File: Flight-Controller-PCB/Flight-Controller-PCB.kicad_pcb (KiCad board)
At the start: 2 copper layers, 50 x 50 mm, 69 parts, among them J1 Power_In, J2 ESC_1, J3 ESC_2, J4 ESC_3, J5 ESC_4, J6 Receiver, J7 Aux, J8 USB_B_Micro, J9 ICSP, Q1 BSS138, Q2 BSS138, SW1 Reset, U1 MCP6001U, U2 ICM-20689, U3 FT232RL, U4 ATmega328P-AU, U5 LM1117-5.0, Y1 16 MHz

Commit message: Power Management and Selection roughed out
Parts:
- removed the C10 at (95.2, 110.5)
- removed the C18 at (95.2, 116.8)
- removed the D2 at (92.4, 99.3)
- removed the D3 at (94.1, 99.3)
- removed D5: Green 2.2V 20mA, LED_SMD:LED_0603_1608Metric_Pad1.05x0.95mm_HandSolder
- removed J9: ICSP, Connector_PinHeader_2.54mm:PinHeader_2x03_P2.54mm_Vertical
- removed the R16 at (92.4, 103.0)
- removed the R17 at (94.2, 103.0)
- removed R21: 1 kohm 5%, Resistor_SMD:R_0603_1608Metric_Pad1.05x0.95mm_HandSolder
- removed R22: 200 ohm 5%, Resistor_SMD:R_0603_1608Metric_Pad1.05x0.95mm_HandSolder
- removed SW1: Reset, Custom:Switch
- added C13: 1uF 16V X7R 10%, Capacitor_SMD:C_0603_1608Metric_Pad1.05x0.95mm_HandSolder, F.Cu at (156.7, 124.2)
- added C7: 22pF 12V X7R 2%, Capacitor_SMD:C_0603_1608Metric_Pad1.05x0.95mm_HandSolder, F.Cu at (154.2, 119.1)
- added R19: 22 ohm 1%, Resistor_SMD:R_0603_1608Metric_Pad1.05x0.95mm_HandSolder, F.Cu at (133.7, 123.4)
- added R20: 22 ohm 1%, Resistor_SMD:R_0603_1608Metric_Pad1.05x0.95mm_HandSolder, F.Cu at (131.8, 120.1)
- added Y1: 16MHz, CL 7pF, Custom:Crystal, F.Cu at (150.9, 125.0)
- C11: value 0.1uF 16V X7R 10% -> 22pF 12V X7R 2%
- U3: value FT232RL -> ATmega32U4-AU; footprint Package_SO:SSOP-28_5.3x10.2mm_P0.65mm -> Package_QFP:TQFP-44_10x10mm_P0.8mm
- moved U3 41.5 mm to (142.5, 116.3), turned to 45 degrees
- moved C11 38.4 mm to (145.3, 126.5), turned to 0 degrees
- renumbered C9 to C10, C13 to C14, C14 to C15, C15 to C16, C16 to C17, C17 to C18, C7 to C8, C8 to C9, D4 to D2, D6 to D3, R18 to R16, R19 to R17, R20 to R18, U5 to U4, Y1 to Y2
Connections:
- net Net-(D1-Pad1) renamed /B_RGB
- net Net-(D1-Pad3) renamed /R_RGB
- net Net-(D1-Pad5) renamed /G_RGB
- C11 pad 1: RESET -> GND
- J6 pad 4: D11 -> Aux_Digital
- J6 pad 6: (no net) -> Aux_Digital
- J7 pad 2: A6 -> A1
- R16 pad 1: RX -> (no net)
- R16 pad 2: Net-(R18-Pad2) -> (no net)
- R17 pad 1: TX -> (no net)
- R17 pad 2: Net-(R19-Pad2) -> (no net)
- R4 pad 1: D12 -> D2
- R5 pad 1: D2 -> (no net)
- R6 pad 1: A1 -> A2
- R7 pad 1: A2 -> A3
- R8 pad 1: A3 -> A6
- U3 pad 1: RX -> (no net)
- U3 pad 14: (no net) -> Net-(U3-Pad14)
- U3 pad 15: Net-(J8-Pad3) -> GND
- U3 pad 16: Net-(J8-Pad2) -> Net-(C11-Pad2)
- U3 pad 17: +3V3 -> Net-(C7-Pad1)
- U3 pad 18: GND -> (no net)
- U3 pad 2: Net-(C11-Pad2) -> (no net)
- U3 pad 20: +5V -> (no net)
- U3 pad 21: GND -> (no net)
- U3 pad 22: Net-(D3-Pad1) -> (no net)
- U3 pad 23: Net-(D2-Pad1) -> GND
- U3 pad 24: (no net) -> Net-(U3-Pad24)
- U3 pad 25: GND -> (no net)
- U3 pad 26: GND -> (no net)
- U3 pad 3: (no net) -> D-
- U3 pad 4: +5V -> D+
- U3 pad 5: TX -> GND
- U3 pad 6: (no net) -> Net-(C13-Pad1)
- U3 pad 7: GND -> (no net)
- U4 pad 15: D11 -> (no net)
- U4 pad 16: D12 -> (no net)
- U4 pad 29: RESET -> (no net)
- U4 pad 30: Net-(R18-Pad2) -> (no net)
- U4 pad 31: Net-(R19-Pad2) -> (no net)
- U4 pad 7: Net-(U4-Pad7) -> (no net)
- U4 pad 8: Net-(U4-Pad8) -> (no net)
- Y2 pad 1: Net-(U4-Pad8) -> (no net)
- Y2 pad 3: Net-(U4-Pad7) -> (no net)
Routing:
- net (no net): track 0.00 -> 122.8 mm, vias 0 -> 7
- net D12: track 57.1 -> 0.00 mm, vias 3 -> 0
- net RESET: track 40.9 -> 0.00 mm, vias 2 -> 0
- net D2: track 21.7 -> 50.9 mm, vias 2 -> 4
- net D11: track 28.7 -> 0.00 mm, vias 2 -> 0
- net Aux_Digital: track 65.1 -> 91.4 mm, vias 3 -> 5
- net Net-(R19-Pad2): track 22.0 -> 0.00 mm, vias 2 -> 0
- net Net-(R18-Pad2): track 14.0 -> 0.00 mm, vias 2 -> 0
- net A6: track 7.56 -> 0.00 mm
- net A1: track 0.00 -> 7.56 mm
- net RX: track 6.81 -> 0.00 mm
- net TX: track 6.71 -> 0.00 mm
- net Net-(U4-Pad8): track 2.82 -> 0.00 mm
- net Net-(U4-Pad7): track 2.81 -> 0.00 mm
- net Net-(D2-Pad2) (its old number): track 1.96 -> 0.00 mm
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
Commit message: Create BOM and schematic
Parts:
- removed the U4 at (88.9, 126.4)
- removed the U4 at (101.9, 103.4)
- removed Y2: 16 MHz, Custom:Resonator
- added C19: 22uF 16V 20%, Capacitor_SMD:C_0603_1608Metric_Pad1.05x0.95mm_HandSolder, F.Cu at (185.8, 138.7)
- added C20: 22uF 16V 20%, Capacitor_SMD:C_0603_1608Metric_Pad1.05x0.95mm_HandSolder, F.Cu at (190.1, 139.0)
- added C21: 0.1uF 16V X7R 10%, Capacitor_SMD:C_0603_1608Metric_Pad1.05x0.95mm_HandSolder, F.Cu at (199.7, 129.5)
- added C22: 1uF 16V X7R 10%, Capacitor_SMD:C_0603_1608Metric_Pad1.05x0.95mm_HandSolder, F.Cu at (196.3, 124.5)
- added D4: 75V 150mA, Diode_SMD:D_0603_1608Metric_Pad1.05x0.95mm_HandSolder, F.Cu at (186.6, 133.7)
- added D5: Orange 2V 20mA, LED_SMD:LED_0603_1608Metric_Pad1.05x0.95mm_HandSolder, F.Cu at (186.7, 126.4)
- added D6: Orange 2V 20mA, LED_SMD:LED_0603_1608Metric_Pad1.05x0.95mm_HandSolder, F.Cu at (177.1, 139.7)
- added FB1: Ferrite 30 ohm 1 line, Diode_SMD:D_0603_1608Metric_Pad1.05x0.95mm_HandSolder, F.Cu at (178.2, 135.8)
- added J9: USB_B_Micro, Connector_USB:USB_Micro-B_Molex-105017-0001, F.Cu at (179.5, 123.6)
- added Q3: PMV48XP,215, Package_TO_SOT_SMD:SOT-23, F.Cu at (186.6, 130.1)
- added Q4: PMV48XP,215, Package_TO_SOT_SMD:SOT-23, F.Cu at (191.9, 122.9)
- added R21: 22 ohm 1%, Resistor_SMD:R_0603_1608Metric_Pad1.05x0.95mm_HandSolder, F.Cu at (190.1, 136.5)
- added RV1: 5V 0.5pF, Diode_SMD:D_0603_1608Metric_Pad1.05x0.95mm_HandSolder, F.Cu at (177.1, 142.3)
- added RV2: 5V 0.5pF, Diode_SMD:D_0603_1608Metric_Pad1.05x0.95mm_HandSolder, F.Cu at (196.3, 122.0)
- added SW1: Push-Switch, Custom:Switch, F.Cu at (179.5, 131.2)
- added U4: LM1117-5.0, Package_TO_SOT_SMD:SOT-223, F.Cu at (165.1, 139.2)
- added U5: LP2985-3.3, Package_TO_SOT_SMD:SOT-23-5, F.Cu at (172.4, 140.7)
- C11: value 22pF 12V X7R 2% -> 1uF 16V X7R 10%
- C12, C18: value 0.1uF 16V X7R 10% -> 1uF 16V X7R 10%
- C13: value 1uF 16V X7R 10% -> 0.1uF 16V X7R 10%
- C14, C15: value 10uF 25V 20% -> 0.1uF 16V X7R 10%
- C16: value 1uF 16V X7R 10% -> 0.1uF 20V X7R 10%
- C17: value 4.7uF 10V 20% -> 10uF 20V 20%
- C4: value 2.2uF 16V X7R 10% -> 0.47uF 16V X7R 10%
- C5: value 0.1uF 16V X7R 10% -> 2.2uF 16V X7R 10%
- C6: value 0.47uF 16V X7R 10% -> 0.1uF 16V X7R 10%
- C8: value 1uF 16V X7R 10% -> 22pF 12V X7R 2%
- C9: value 4.7uF 10V 20% -> 0.1uF 16V X7R 10%
- D3: value SS1P3L -> Green 2.2V 20mA; footprint Custom:SS1P3L -> LED_SMD:LED_0603_1608Metric_Pad1.05x0.95mm_HandSolder
- J1: value Power_In -> ESC_1; footprint Connector_JST:JST_GH_BM06B-GHS-TBT_1x06-1MP_P1.25mm_Vertical -> Connector_JST:JST_GH_BM05B-GHS-TBT_1x05-1MP_P1.25mm_Vertical
- J2: value ESC_1 -> Receiver; footprint Connector_JST:JST_GH_BM04B-GHS-TBT_1x04-1MP_P1.25mm_Vertical -> Connector_JST:JST_GH_BM07B-GHS-TBT_1x07-1MP_P1.25mm_Vertical
- J3: footprint Connector_JST:JST_GH_BM04B-GHS-TBT_1x04-1MP_P1.25mm_Vertical -> Connector_JST:JST_GH_BM05B-GHS-TBT_1x05-1MP_P1.25mm_Vertical
- J4: value ESC_3 -> ICSP; footprint Connector_JST:JST_GH_BM04B-GHS-TBT_1x04-1MP_P1.25mm_Vertical -> Connector_PinHeader_2.54mm:PinHeader_2x03_P2.54mm_Vertical
- J5: value ESC_4 -> ESC_3; footprint Connector_JST:JST_GH_BM04B-GHS-TBT_1x04-1MP_P1.25mm_Vertical -> Connector_JST:JST_GH_BM05B-GHS-TBT_1x05-1MP_P1.25mm_Vertical
- J6: value Receiver -> Aux; footprint Connector_JST:JST_GH_BM07B-GHS-TBT_1x07-1MP_P1.25mm_Vertical -> Connector_JST:JST_GH_BM04B-GHS-TBT_1x04-1MP_P1.25mm_Vertical
- J7: value Aux -> ESC_4; footprint Connector_JST:JST_GH_BM04B-GHS-TBT_1x04-1MP_P1.25mm_Vertical -> Connector_JST:JST_GH_BM05B-GHS-TBT_1x05-1MP_P1.25mm_Vertical
- J8: value USB_B_Micro -> Power_In; footprint Connector_USB:USB_Micro-B_Molex-105017-0001 -> Connector_JST:JST_GH_BM06B-GHS-TBT_1x06-1MP_P1.25mm_Vertical
- R15: value 10 kohm 5% -> 1 kohm 5%
- R17: value 1 kohm 5% -> 10 kohm 5%
- R18: value 150 ohm 5% -> 10 kohm 5%
- R19: value 22 ohm 1% -> 10 kohm 5%
- R6: value ?? ohm 5% -> 150 ohm 5%
- R7: value ?? ohm 5% -> 55 ohm 5%
- R8, R9: value ?? ohm 5% -> 10 kohm 5%
- moved R15 116.8 mm to (200.6, 124.5), turned to 0 degrees
- moved R14 112.4 mm to (195.4, 127.0)
- moved C9 109.3 mm to (191.0, 126.5), turned to 0 degrees
- moved C8 109.2 mm to (191.0, 129.0)
- moved C14 106.2 mm to (194.5, 137.1)
- moved C10 106.0 mm to (200.7, 121.9), turned to 0 degrees
- moved R18 105.8 mm to (181.4, 143.4), turned to 0 degrees
- moved C12 104.9 mm to (199.7, 132.0), turned to 0 degrees
- moved C15 102.9 mm to (195.3, 132.0), turned to 0 degrees
- moved U1 102.7 mm to (177.3, 94.5), turned to 0 degrees
- moved C1 98.1 mm to (177.1, 98.1), turned to 0 degrees
- moved R16 97.7 mm to (195.3, 129.5), turned to 0 degrees
- moved C16 97.0 mm to (191.0, 131.5), turned to 0 degrees
- moved R1 94.6 mm to (170.3, 110.8), turned to 0 degrees
- moved C2 93.6 mm to (171.3, 103.7), turned to 0 degrees
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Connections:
- C10 pad 1: +5V -> Net-(C10-Pad1)
- C11 pad 1: GND -> +5V
- C11 pad 2: Net-(C11-Pad2) -> GND
- C12 pad 1: Net-(C12-Pad1) -> +5V
- C13 pad 1: Net-(C13-Pad1) -> +5V
- C14 pad 1: VDD -> +5V
- C15 pad 1: +5V -> VBUS
- C16 pad 1: +5V -> Net-(C16-Pad1)
- C17 pad 1: VBUS -> Net-(C16-Pad1)
- C18 pad 1: VBUS -> +5V
- C4 pad 1: +3V3 -> Net-(C4-Pad1)
- C5 pad 1: GND -> +3V3
- C5 pad 2: +3V3 -> GND
- C6 pad 1: Net-(C6-Pad1) -> GND
- C6 pad 2: GND -> +3V3
- C8 pad 2: +5V -> Net-(C8-Pad2)
- C9 pad 1: +5V -> Net-(C9-Pad1)
- D3 pad 1: +5V -> GND
- D3 pad 2: VBUS -> Net-(D3-Pad2)
- F1 pad 1: Net-(F1-Pad1) -> Net-(C20-Pad1)
- J1 pad 2: GND -> A1
- J1 pad 4: VDD -> D4
- J1 pad 5: VDD -> +5V
- J2 pad 2: Net-(J2-Pad2) -> D15-SCK
- J2 pad 3: D4 -> D16-MOSI
- J2 pad 4: +5V -> D8
- J3 pad 2: Net-(J3-Pad2) -> A2
- J3 pad 3: D5 -> GND
- J3 pad 4: +5V -> D5
- J4 pad 1: GND -> D14-MISO
- J4 pad 2: Net-(J4-Pad2) -> +5V
- J4 pad 3: D6 -> D15-SCK
- J4 pad 4: +5V -> D16-MOSI
- J5 pad 2: Net-(J5-Pad2) -> A3
- J5 pad 3: D7 -> GND
- J5 pad 4: +5V -> D6
- J6 pad 2: D8 -> A5
- J6 pad 3: D9 -> Aux_Digital
- J6 pad 4: Aux_Digital -> +5V
- J7 pad 2: A1 -> A4
- J7 pad 3: Aux_Digital -> GND
- J7 pad 4: +5V -> D7
- J8 pad 1: Net-(F1-Pad1) -> GND
- J8 pad 2: Net-(J8-Pad2) -> GND
- J8 pad 3: Net-(J8-Pad3) -> GND
- J8 pad 4: (no net) -> VDD
- J8 pad 5: GND -> VDD
- J8 pad 6: GND -> VDD
- Q1 pad 3: A5_SCL -> IMU_SCL_LH
- Q2 pad 3: A4_SDA -> IMU_SDA_LH
- R10 pad 1: IMU_SCL_LL -> IMU_SCL_LH
- R10 pad 2: +3V3 -> +5V
- R11 pad 1: IMU_SCL_LL -> IMU_SDA_LL
- R12 pad 1: A5_SCL -> IMU_SDA_LL
- R12 pad 2: +5V -> +3V3
- R13 pad 1: IMU_SDA_LL -> IMU_SDA_LH
- R13 pad 2: +3V3 -> +5V
- R14 pad 1: IMU_SDA_LL -> RESET
- R14 pad 2: +3V3 -> +5V
- R15 pad 1: A4_SDA -> Net-(R15-Pad1)
- R15 pad 2: +5V -> Net-(D5-Pad2)
- R16 pad 1: (no net) -> Net-(R16-Pad1)
- R16 pad 2: (no net) -> Net-(D6-Pad2)
- R17 pad 1: (no net) -> Net-(R17-Pad1)
- R17 pad 2: (no net) -> GND
- R18 pad 1: Net-(D2-Pad2) -> GND
- R18 pad 2: +5V -> VDD
- R19 pad 1: Net-(J8-Pad3) -> GND
- R19 pad 2: D+ -> VBUS
- R20 pad 1: D- -> D+
- R20 pad 2: Net-(J8-Pad2) -> D+
- R4 pad 1: D2 -> D11
- R5 pad 1: (no net) -> D12
- R6 pad 1: A2 -> +5V
- R6 pad 2: Net-(J2-Pad2) -> Net-(D2-Pad2)
- R7 pad 1: A3 -> +3V3
- R7 pad 2: Net-(J3-Pad2) -> Net-(D3-Pad2)
- R8 pad 1: A6 -> IMU_SCL_LL
- R8 pad 2: Net-(J4-Pad2) -> +3V3
- R9 pad 1: A7 -> IMU_SCL_LL
- R9 pad 2: Net-(J5-Pad2) -> +3V3
- U2 pad 10: Net-(C6-Pad1) -> Net-(C4-Pad1)
- U2 pad 12: (no net) -> Net-(U2-Pad12)
- U2 pad 22: (no net) -> Net-(U2-Pad22)
- U3 pad 1: (no net) -> D7
- U3 pad 10: (no net) -> D16-MOSI
- U3 pad 11: (no net) -> D14-MISO
- U3 pad 12: (no net) -> D11
- U3 pad 13: (no net) -> RESET
- U3 pad 14: Net-(U3-Pad14) -> +5V
- U3 pad 16: Net-(C11-Pad2) -> Net-(C8-Pad2)
- U3 pad 18: (no net) -> IMU_SCL_LH
- U3 pad 19: (no net) -> IMU_SDA_LH
- U3 pad 2: (no net) -> +5V
- U3 pad 20: (no net) -> RX
- U3 pad 21: (no net) -> TX
- U3 pad 22: (no net) -> Net-(R16-Pad1)
- U3 pad 24: Net-(U3-Pad24) -> +5V
- U3 pad 25: (no net) -> D4
- U3 pad 26: (no net) -> D12
- U3 pad 27: (no net) -> D6
- U3 pad 28: (no net) -> D8
- U3 pad 29: (no net) -> D8
- U3 pad 30: (no net) -> Aux_Digital
- U3 pad 31: (no net) -> D5
- U3 pad 32: (no net) -> B_RGB_LED
- U3 pad 33: (no net) -> Net-(R17-Pad1)
- U3 pad 34: Net-(U3-Pad14) -> +5V
- U3 pad 36: (no net) -> A0
- U3 pad 37: (no net) -> A1
- U3 pad 38: (no net) -> A2
- U3 pad 39: (no net) -> A3
- U3 pad 40: (no net) -> A4
- U3 pad 41: (no net) -> A5
- U3 pad 42: Net-(C12-Pad1) -> Net-(C9-Pad1)
- U3 pad 44: Net-(U3-Pad24) -> +5V
- U3 pad 6: Net-(C13-Pad1) -> Net-(C10-Pad1)
- U3 pad 7: (no net) -> VBUS
- U3 pad 8: (no net) -> Net-(R15-Pad1)
- U3 pad 9: (no net) -> D15-SCK
- Y1 pad -: GND -> (no net)
- Y1 pad 1: Net-(C11-Pad2) -> Net-(C8-Pad2)
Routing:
- net +5V: track 263.6 -> 0.00 mm, vias 6 -> 0
- net (no net): track 122.8 -> 0.00 mm, vias 7 -> 0
- net Aux_Digital: track 91.4 -> 0.00 mm, vias 5 -> 0
- net D2: track 50.9 -> 0.00 mm, vias 4 -> 0
- net +3V3: track 46.7 -> 0.00 mm
- net VDD: track 34.8 -> 0.00 mm
- net D7: track 25.5 -> 0.00 mm
- net D6: track 24.6 -> 0.00 mm, vias 2 -> 0
- net Net-(D2-Pad1): track 24.3 -> 0.00 mm, vias 2 -> 0
- net A3: track 23.3 -> 0.00 mm
- net B_RGB_LED: track 23.2 -> 0.00 mm, vias 2 -> 0
- net A5_SCL: track 23.0 -> 0.00 mm
- net Net-(D3-Pad1): track 19.8 -> 0.00 mm, vias 2 -> 0
- net Net-(J8-Pad2): track 16.1 -> 0.00 mm
- net Net-(J8-Pad3): track 15.9 -> 0.00 mm
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
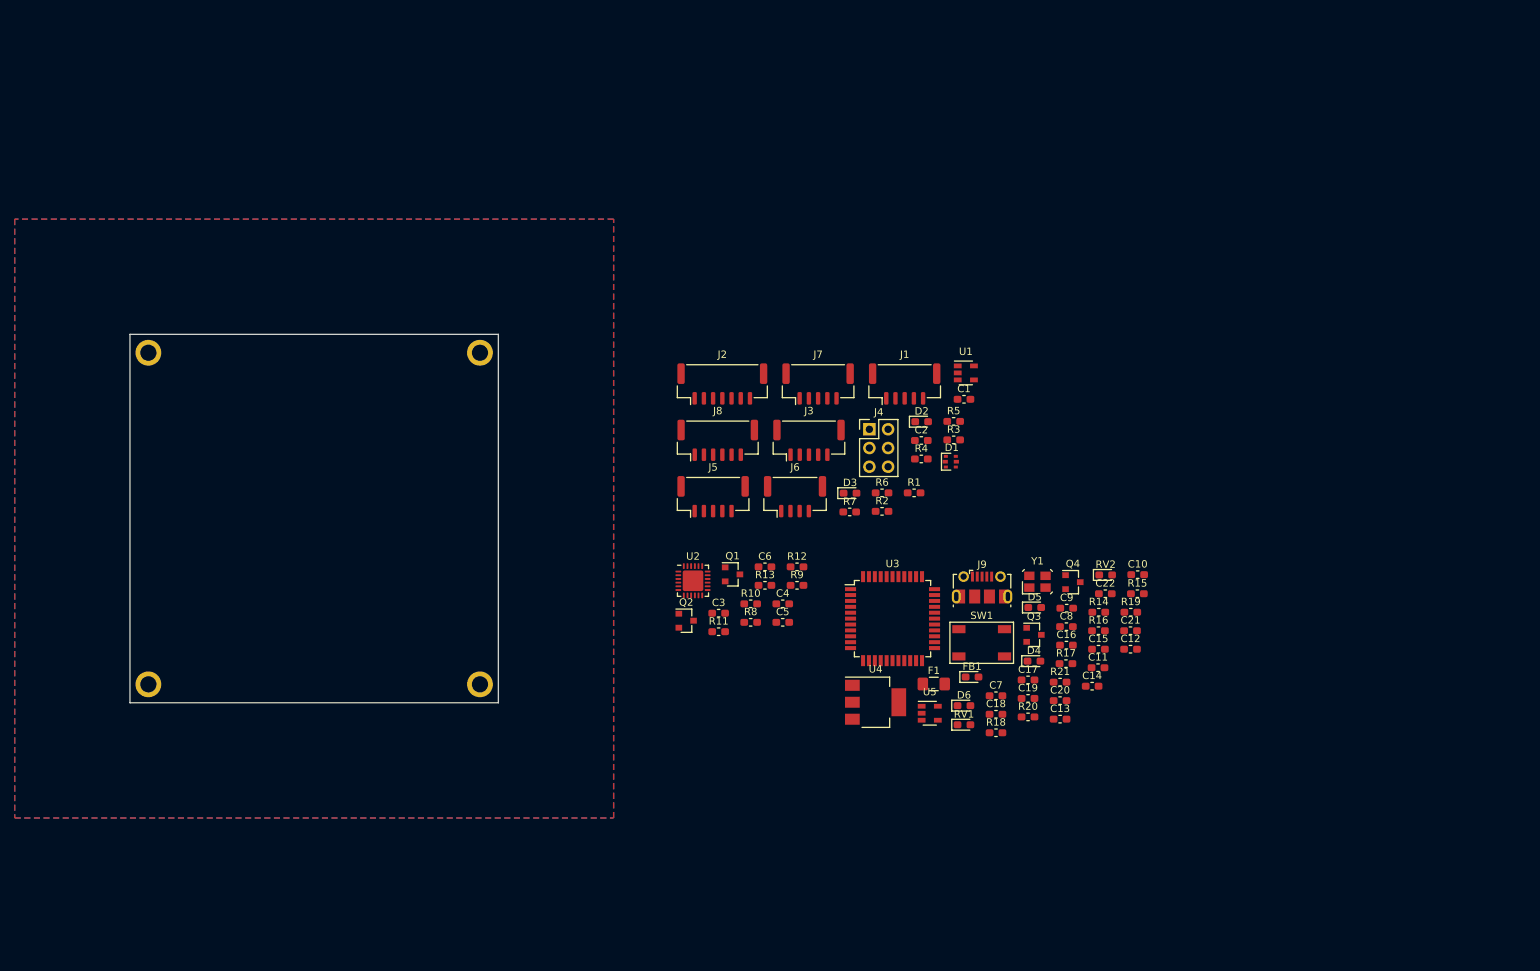
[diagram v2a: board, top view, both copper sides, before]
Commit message: Group components
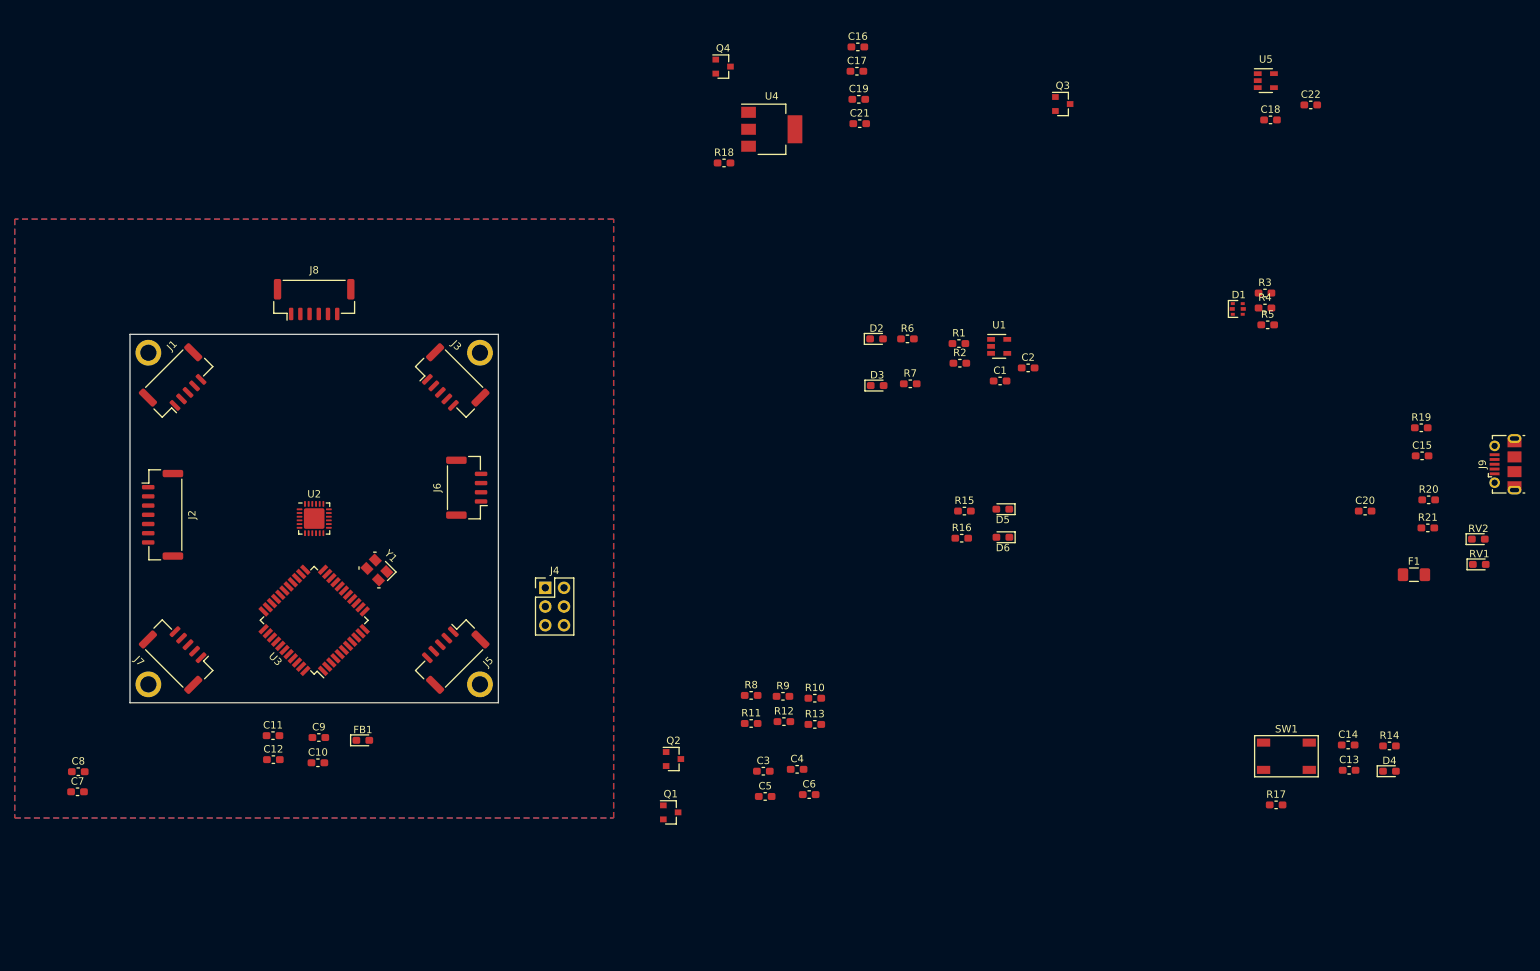
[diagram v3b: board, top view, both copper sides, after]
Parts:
- moved C8 135.5 mm to (56.9, 148.7)
- moved C7 125.3 mm to (56.8, 151.4)
- moved C12 117.3 mm to (83.4, 147.0)
- moved C10 114.1 mm to (89.4, 147.4)
- moved C11 112.4 mm to (83.3, 143.8)
- moved C9 103.0 mm to (89.5, 144.0)
- moved J1 98.6 mm to (70.4, 95.8), turned to 45 degrees
- moved U5 97.2 mm to (218.1, 54.9)
- moved J7 94.4 mm to (70.4, 132.8), turned to 135 degrees
- moved Y1 89.7 mm to (97.4, 121.3), turned to 135 degrees
- moved C18 88.9 mm to (218.7, 60.2)
- moved C16 86.0 mm to (162.7, 50.3)
- moved C17 85.8 mm to (162.6, 53.6)
- moved R18 85.7 mm to (144.5, 66.0)
- moved Q4 84.6 mm to (144.4, 53.0)
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
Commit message: Placed the crystal and IMU is mostly routed
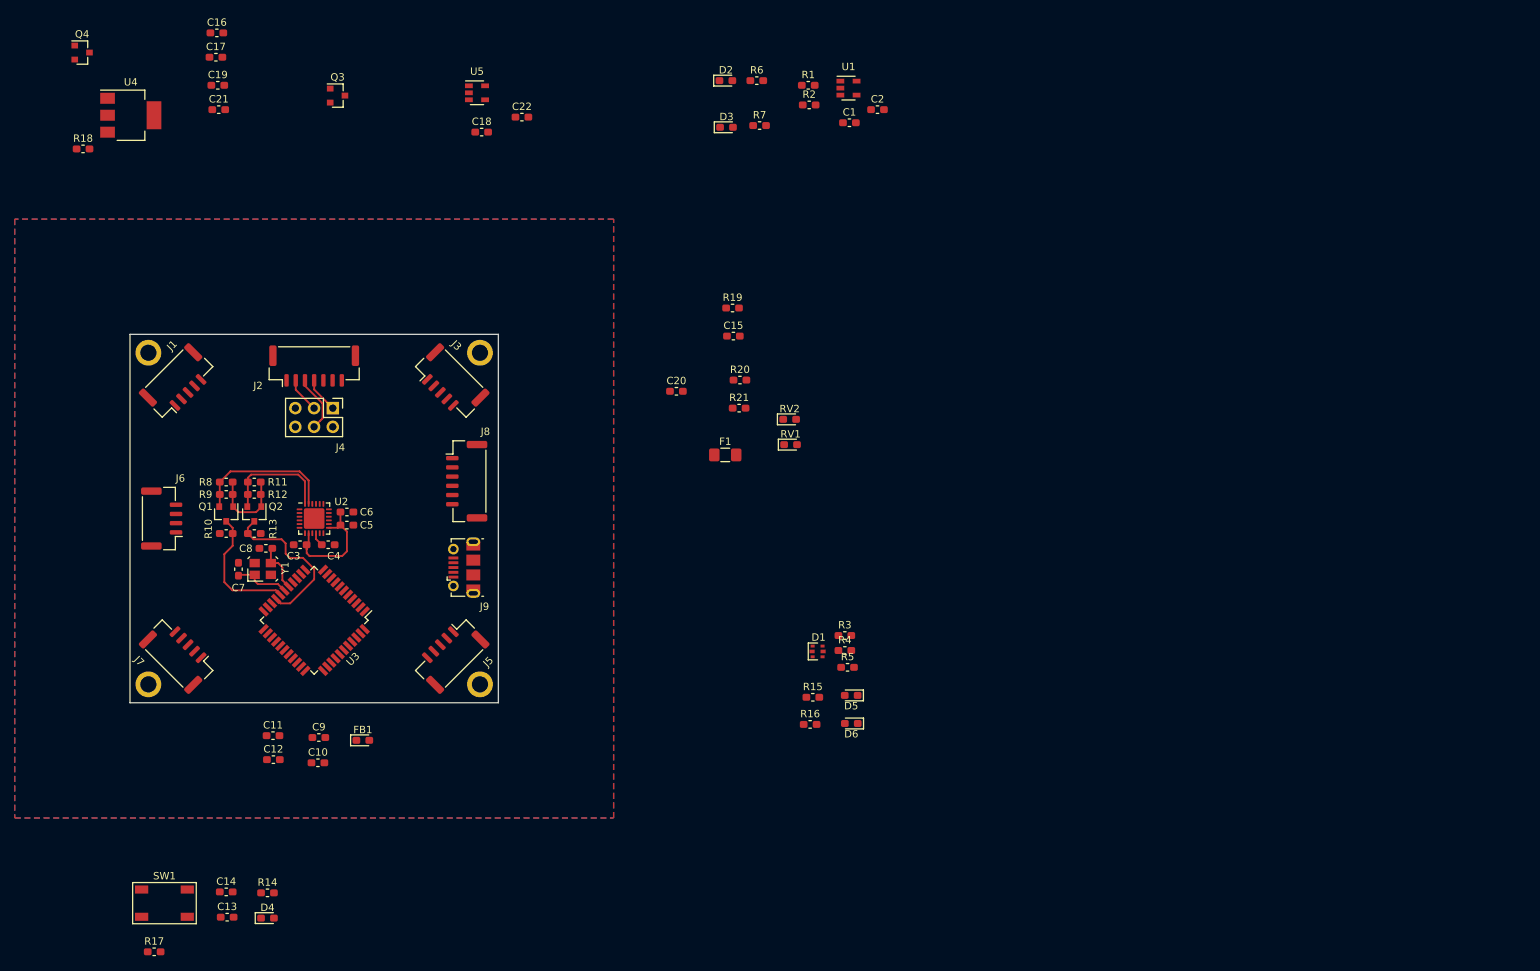
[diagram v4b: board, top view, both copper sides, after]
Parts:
- moved C14 153.6 mm to (77.0, 165.0)
- moved SW1 153.6 mm to (68.6, 166.5)
- moved C13 153.6 mm to (77.1, 168.4)
- moved D4 153.6 mm to (82.6, 168.5)
- moved R14 153.6 mm to (82.6, 165.1)
- moved R17 153.6 mm to (67.2, 173.1)
- moved J9 142.0 mm to (109.3, 120.9)
- moved C22 107.1 mm to (117.1, 59.8)
- moved C18 107.1 mm to (111.6, 61.8)
- moved U5 107.1 mm to (111.0, 56.5)
- moved Q3 98.4 mm to (92.1, 56.9)
- moved C15 94.9 mm to (145.8, 89.5)
- moved C20 94.9 mm to (138.1, 97.0)
- moved R19 94.9 mm to (145.7, 85.7)
- moved R20 94.9 mm to (146.7, 95.5)
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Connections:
- J2 pad 4: D8 -> D14-MISO
- J2 pad 5: D14-MISO -> D8
- J2 pad 6: D8 -> D9
- U3 pad 29: D8 -> D9
- Y1 pad -: (no net) -> GND
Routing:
- net +3V3: track 0.00 -> 27.4 mm
- net IMU_SDA_LH: track 0.00 -> 22.0 mm
- net IMU_SCL_LL: track 0.00 -> 19.7 mm
- net IMU_SCL_LH: track 0.00 -> 17.4 mm
- net IMU_SDA_LL: track 0.00 -> 15.3 mm
- net D16-MOSI: track 0.00 -> 7.78 mm
- net Net-(C7-Pad1): track 0.00 -> 7.66 mm
- net Net-(C8-Pad2): track 0.00 -> 6.83 mm
- net D14-MISO: track 0.00 -> 4.81 mm
- net D15-SCK: track 0.00 -> 4.80 mm
- net Net-(C4-Pad1): track 0.00 -> 1.89 mm
